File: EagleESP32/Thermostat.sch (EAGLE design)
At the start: 61 parts, among them K1 AQY282EHA, K2 AQY282EHA, K3 AQY282EHA, K4 AQY282EHA, K5 AQY282EHA, Q1 MOSFET-NCHANNELAO3404A, U1 ESP-WROOM-03, X1 1751303

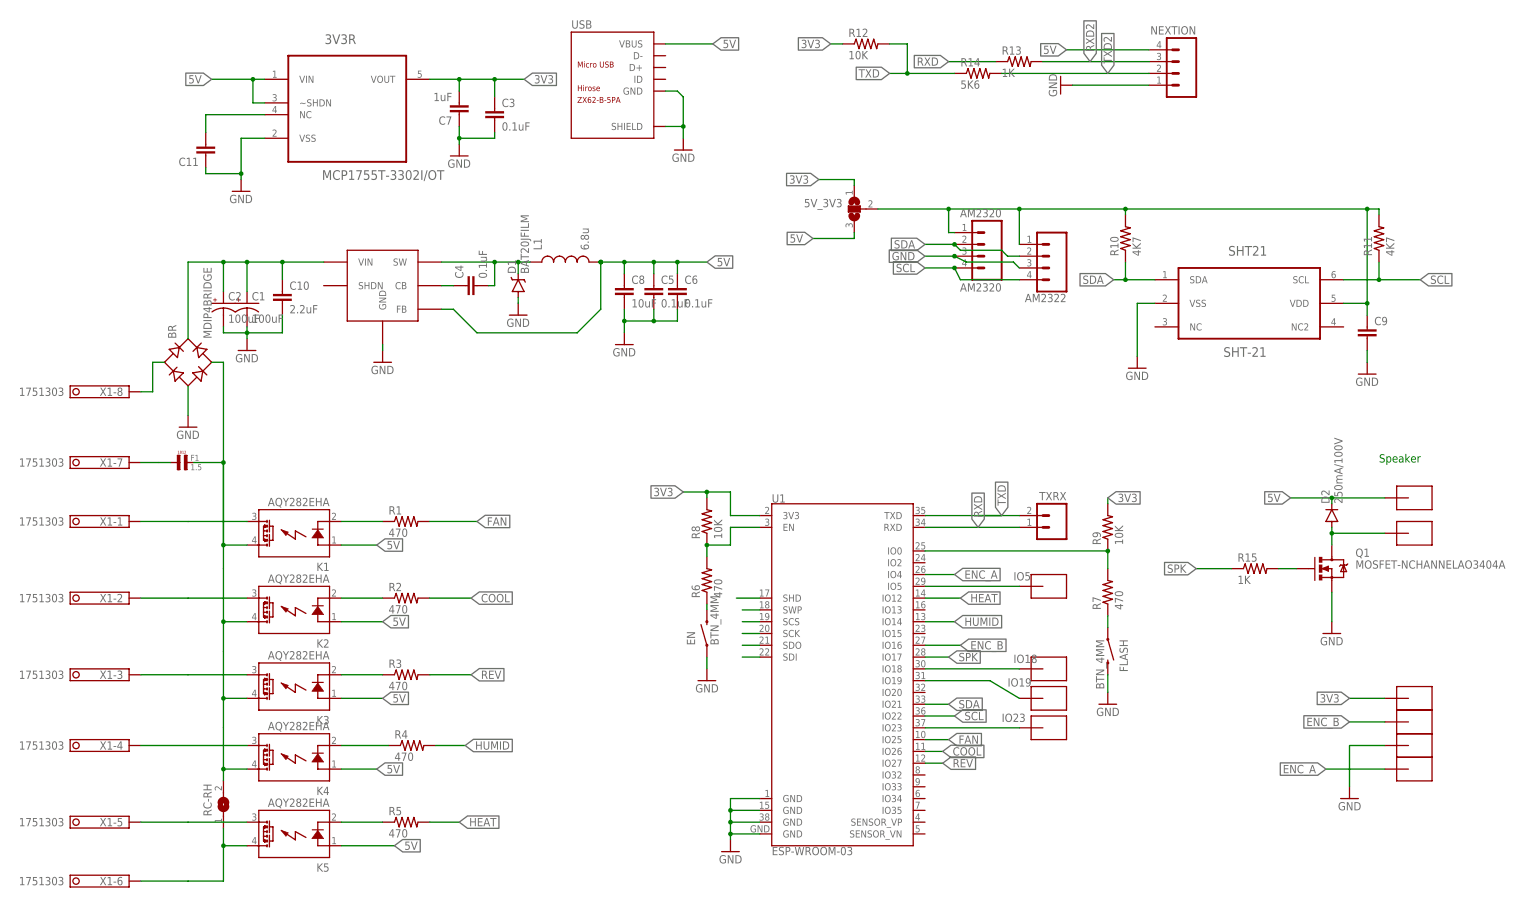
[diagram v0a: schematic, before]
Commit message: rev 1. GPIO12 is connected to 1.3V LDO (r0 failed!)
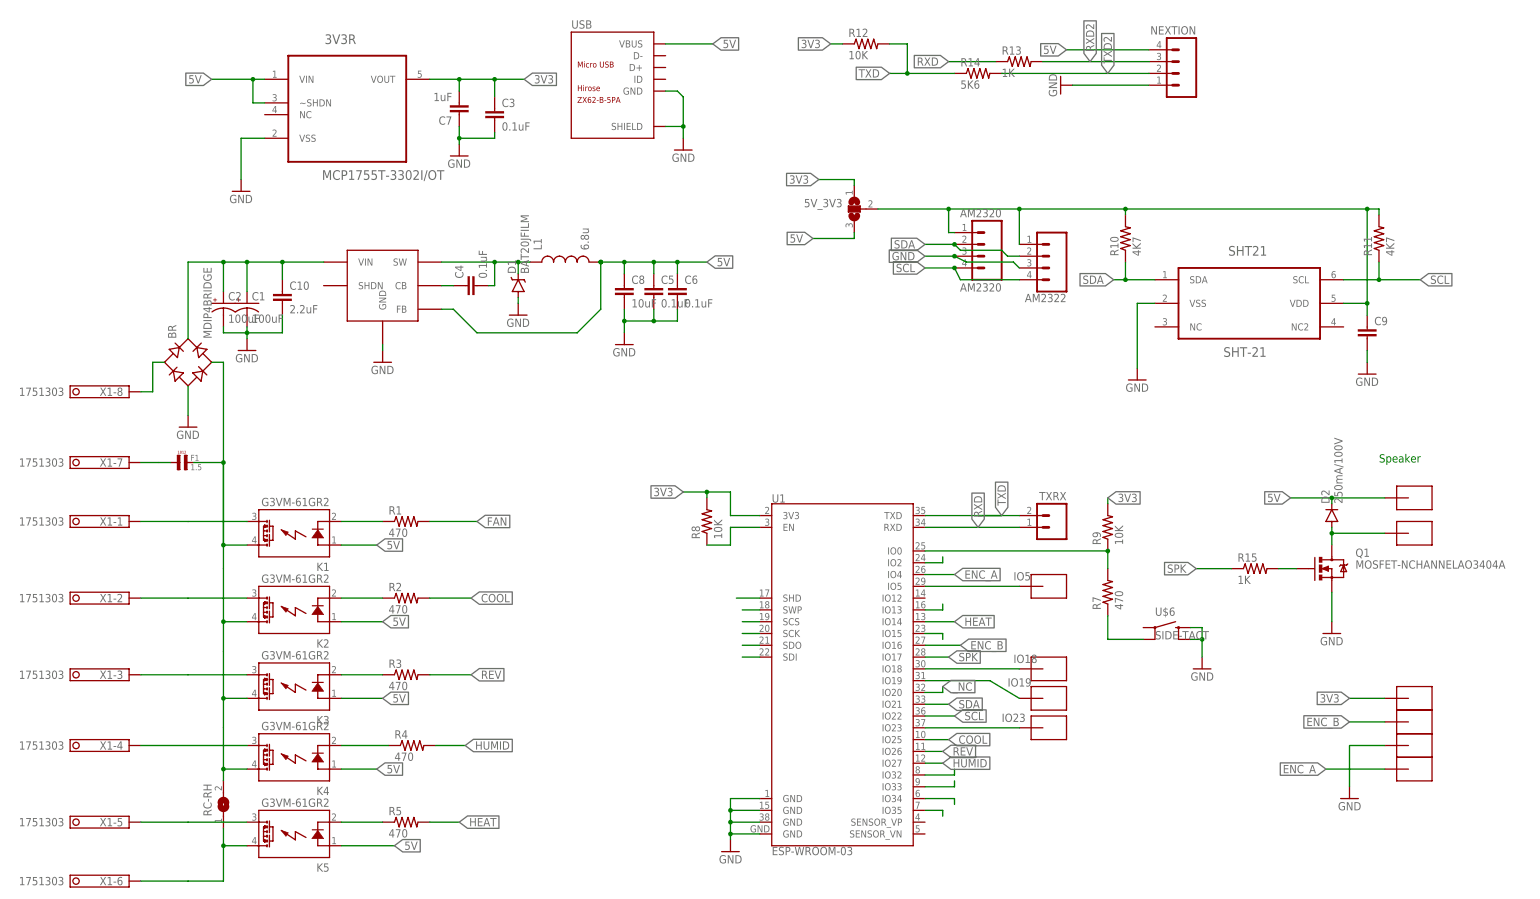
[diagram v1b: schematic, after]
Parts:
- removed C11: (no value), SparkFun-Capacitors:CAP0805
- removed EN, FLASH: BTN_4MM, CuriousTech:BTN_4MM
- removed R6: 470, SparkFun-Resistors:RESISTOR0805-RES
- added U$6: SIDE-TACT, CuriousTech:SIDE-TACT
- K1, K2, K3, K4, K5: value AQY282EHA -> G3VM-61GR2
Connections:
- removed net N$28: EN.2, R6.1
- removed net N$34: 3V3R.NC, C11.2
- new net N$35: U1.IO2
- new net N$36: U1.IO13
- new net N$37: U1.IO15
- new net N$40: U1.IO32
- new net N$42: U1.IO34
- new net N$43: U1.IO35
- new net _NC: U1.IO20
- net COOL: now also U1.IO25; no longer U1.IO26
- net FAN: now also U1.IO33; no longer U1.IO25
- net GND: now also U$6.2, U$6.4; no longer C11.1, EN.1, FLASH.2
- net HEAT: now also U1.IO14; no longer U1.IO12
- net HUMID: now also U1.IO27; no longer U1.IO14
- net N$27: now also U$6.3; no longer FLASH.1
- net N$9: no longer R6.2
- net REV: now also U1.IO26; no longer U1.IO27

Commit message: Worst mistake ever. I quit.
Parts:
- removed C2: 100uF, SparkFun-Capacitors:CAP_POLC
- R14: value 5K6 -> 5K1
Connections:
- net 3V3: now also K1.A, K2.A, K3.A, K4.A, K5.A
- net 5V: no longer K1.A, K2.A, K3.A, K4.A, K5.A
- net GND: no longer C2.-
- net N$24: no longer C2.+
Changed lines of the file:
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@@
 <part name="C3" library="SparkFun-Capacitors" deviceset="CAP" device="0805" value="0.1uF"/>
 <part name="3V3R" library="Microchip_By_element14_Batch_1" deviceset="MCP1801T-3302I/OT" device="" value="MCP1755T-3302I/OT"/>
-<part name="R14" library="SparkFun-Resistors" deviceset="RESISTOR" device="0805-RES" value="5K6"/>
+<part name="R14" library="SparkFun-Resistors" deviceset="RESISTOR" device="0805-RES" value="5K1"/>
 <part name="K4" library="relay" deviceset="AQY*" device="SOP" technology="22" value="G3VM-61GR2"/>
 <part name="GND26" library="supply1" deviceset="GND" device=""/>
@@
 <part name="BR" library="CuriousTech" deviceset="MDIP4BRIDGE" device=""/>
 <part name="GND13" library="supply1" deviceset="GND" device=""/>
-<part name="C2" library="SparkFun-Capacitors" deviceset="CAP_POL" device="C" value="100uF"/>
 <part name="AM2320" library="SparkFun-Connectors" deviceset="M04" device="PTH" value="AM2320"/>
 <part name="X1" library="con-phoenix-350" library_urn="urn:adsk.eagle:library:174" deviceset="1751303" device="" package3d_urn="urn:adsk.eagle:package:9408/1"/>
@@
 <attribute name="VALUE" x="288.29" y="26.67" size="1.778" layer="96" rot="MR0"/>
 </instance>
-<instance part="C2" gate="G$1" x="43.18" y="135.89" smashed="yes">
-<attribute name="NAME" x="44.196" y="136.525" size="1.778" layer="95"/>
-<attribute name="VALUE" x="44.196" y="131.699" size="1.778" layer="96"/>
-</instance>
 <instance part="AM2320" gate="G$1" x="205.74" y="148.59" smashed="yes" rot="R180">
 <attribute name="VALUE" x="210.82" y="156.21" size="1.778" layer="96" rot="R180"/>
@@
 <junction x="48.26" y="129.54"/>
 <pinref part="C10" gate="G$1" pin="2"/>
-<wire x1="48.26" y1="129.54" x2="43.18" y2="129.54" width="0.1524" layer="91"/>
-<pinref part="C2" gate="G$1" pin="-"/>
-<wire x1="43.18" y1="129.54" x2="43.18" y2="130.81" width="0.1524" layer="91"/>
 </segment>
 <segment>
@@
 <net name="N$24" class="0">
 <segment>
-<wire x1="48.26" y1="144.78" x2="43.18" y2="144.78" width="0.1524" layer="91"/>
-<wire x1="43.18" y1="144.78" x2="35.56" y2="144.78" width="0.1524" layer="91"/>
+<wire x1="48.26" y1="144.78" x2="35.56" y2="144.78" width="0.1524" layer="91"/>
 <wire x1="35.56" y1="144.78" x2="35.56" y2="128.27" width="0.1524" layer="91"/>
 <wire x1="48.26" y1="138.43" x2="48.26" y2="144.78" width="0.1524" layer="91"/>
@@
 <pinref part="C10" gate="G$1" pin="1"/>
 <pinref part="BR" gate="G$1" pin="+"/>
-<pinref part="C2" gate="G$1" pin="+"/>
-<wire x1="43.18" y1="138.43" x2="43.18" y2="144.78" width="0.1524" layer="91"/>
-<junction x="43.18" y="144.78"/>
 </segment>
 </net>
@@
 <wire x1="194.31" y1="31.75" x2="200.66" y2="31.75" width="0.1524" layer="91"/>
 <wire x1="200.66" y1="31.75" x2="200.66" y2="33.02" width="0.1524" layer="91"/>
+<label x="200.66" y="33.02" size="1.778" layer="95" xref="yes"/>
 </segment>
 </net>
@@
 <wire x1="233.68" y1="92.71" x2="233.68" y2="93.98" width="0.1524" layer="91"/>
 <label x="233.68" y="93.98" size="1.778" layer="95" xref="yes"/>
+</segment>
+<segment>
+<pinref part="K5" gate="G$1" pin="A"/>
+<wire x1="68.58" y1="19.05" x2="80.01" y2="19.05" width="0.1524" layer="91"/>
+<label x="80.01" y="19.05" size="1.778" layer="95" xref="yes"/>
+</segment>
+<segment>
+<pinref part="K4" gate="G$1" pin="A"/>
+<wire x1="68.58" y1="35.56" x2="76.2" y2="35.56" width="0.1524" layer="91"/>
+<label x="76.2" y="35.56" size="1.778" layer="95" xref="yes"/>
+</segment>
+<segment>
+<pinref part="K3" gate="G$1" pin="A"/>
+<wire x1="68.58" y1="50.8" x2="77.47" y2="50.8" width="0.1524" layer="91"/>
+<label x="77.47" y="50.8" size="1.778" layer="95" xref="yes"/>
+</segment>
+<segment>
+<pinref part="K2" gate="G$1" pin="A"/>
+<wire x1="68.58" y1="67.31" x2="77.47" y2="67.31" width="0.1524" layer="91"/>
+<label x="77.47" y="67.31" size="1.778" layer="95" xref="yes"/>
+</segment>
+<segment>
+<pinref part="K1" gate="G$1" pin="A"/>
+<wire x1="68.58" y1="83.82" x2="76.2" y2="83.82" width="0.1524" layer="91"/>
+<label x="76.2" y="83.82" size="1.778" layer="95" xref="yes"/>
 </segment>
 </net>
@@
 <pinref part="D2" gate="G$1" pin="C"/>
 </segment>
-<segment>
-<pinref part="K1" gate="G$1" pin="A"/>
-<wire x1="68.58" y1="83.82" x2="76.2" y2="83.82" width="0.1524" layer="91"/>
-<label x="76.2" y="83.82" size="1.778" layer="95" xref="yes"/>
-</segment>
-<segment>
-<pinref part="K2" gate="G$1" pin="A"/>
-<wire x1="68.58" y1="67.31" x2="77.47" y2="67.31" width="0.1524" layer="91"/>
-<label x="77.47" y="67.31" size="1.778" layer="95" xref="yes"/>
-</segment>
-<segment>
-<pinref part="K3" gate="G$1" pin="A"/>
-<wire x1="68.58" y1="50.8" x2="77.47" y2="50.8" width="0.1524" layer="91"/>
-<label x="77.47" y="50.8" size="1.778" layer="95" xref="yes"/>
-</segment>
-<segment>
-<pinref part="K4" gate="G$1" pin="A"/>
-<wire x1="68.58" y1="35.56" x2="76.2" y2="35.56" width="0.1524" layer="91"/>
-<label x="76.2" y="35.56" size="1.778" layer="95" xref="yes"/>
-</segment>
-<segment>
-<pinref part="K5" gate="G$1" pin="A"/>
-<wire x1="68.58" y1="19.05" x2="80.01" y2="19.05" width="0.1524" layer="91"/>
-<label x="80.01" y="19.05" size="1.778" layer="95" xref="yes"/>
-</segment>
-</net>
+</net>
